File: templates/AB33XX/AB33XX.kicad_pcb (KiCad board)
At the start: 2 copper layers, 170 x 100 mm, 7 parts, among them P1 HE10_2X13

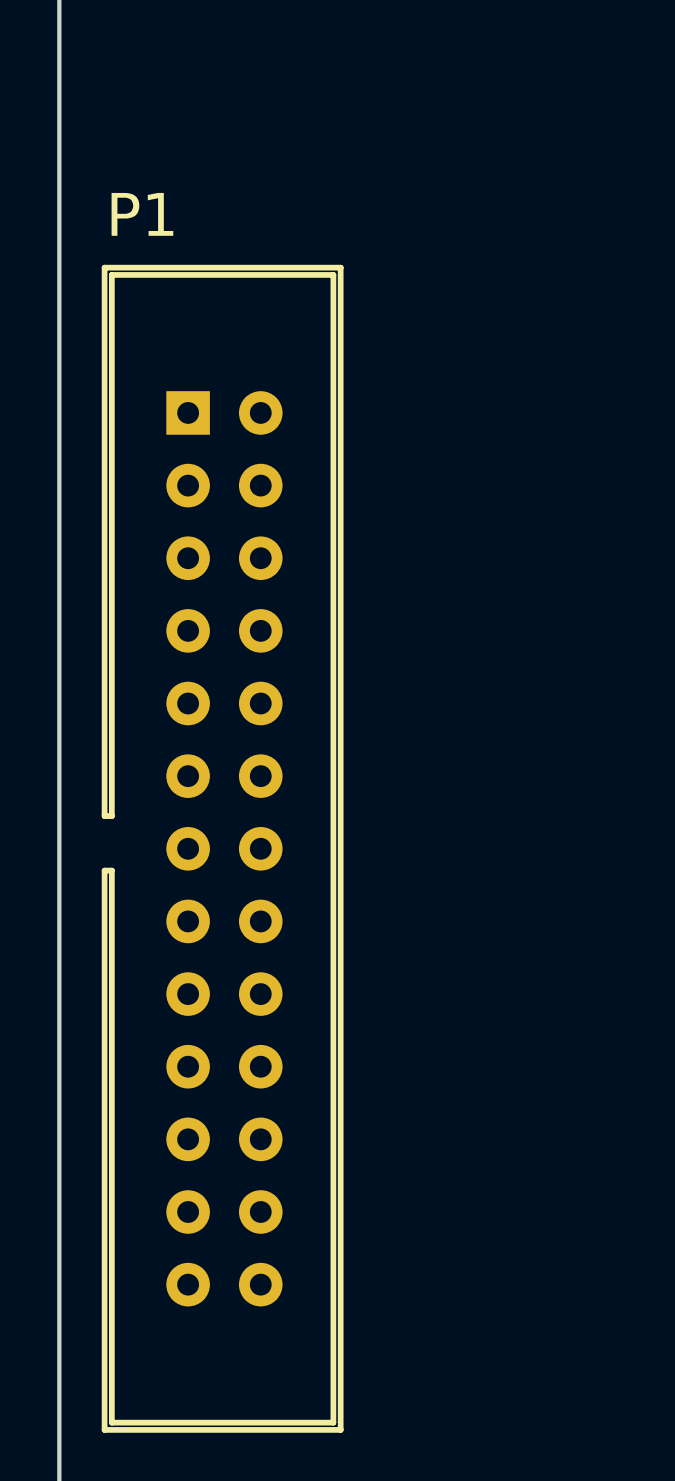
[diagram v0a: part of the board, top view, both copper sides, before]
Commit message: Modify the HE10 and HE14 footprints. Modify the AP33XX template
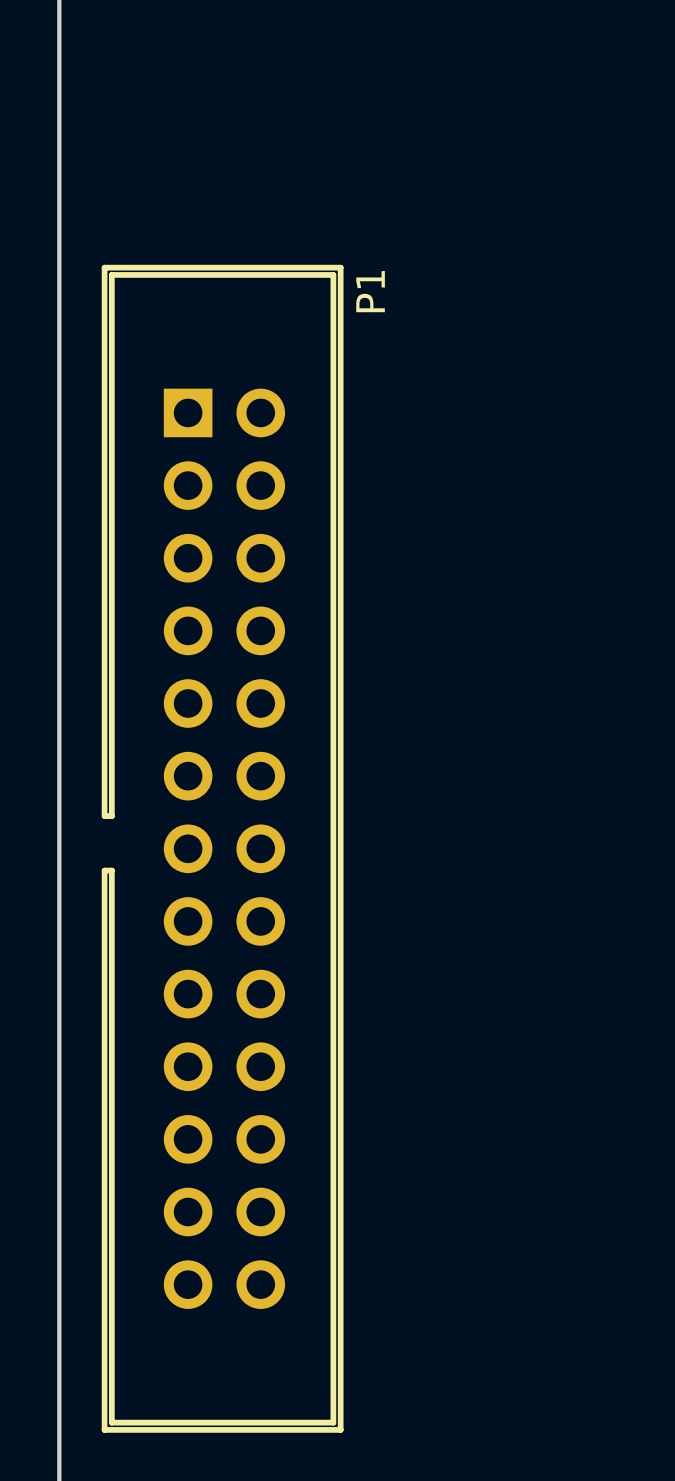
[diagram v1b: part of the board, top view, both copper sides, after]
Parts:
- P1: footprint Apex:HE10_2x13 -> Apex:HE10-V-26
